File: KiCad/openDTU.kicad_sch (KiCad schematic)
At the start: 48 parts, among them J1 USB_C_Receptacle_USB2.0, J2 Conn_Coaxial, J3 Micro_SD_Card, J4 Conn_02x05_Counter_Clockwise, Q1 BC817, Q2 BC817, SW1 SW_Push, SW2 SW_Push, U1 CH340C, U3 ESP32-WROOM-32, U4 nRF24L01P, U5 NCP1117-3.3_SOT223, Y1 16 MHz

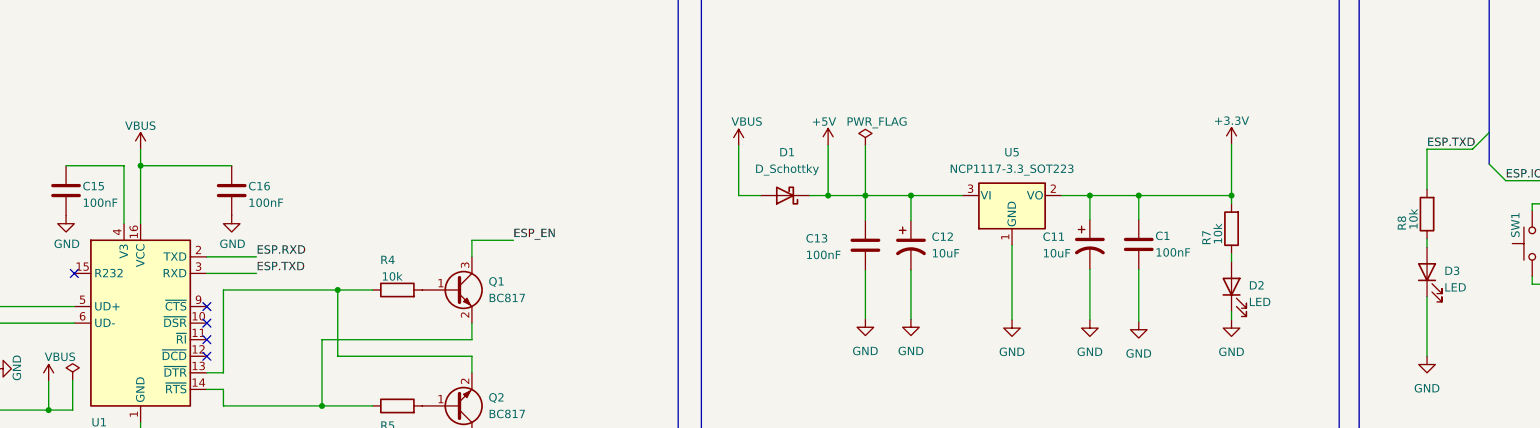
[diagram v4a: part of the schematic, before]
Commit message: fixing bug with wrong voltage at USB-Seriell Interface IC
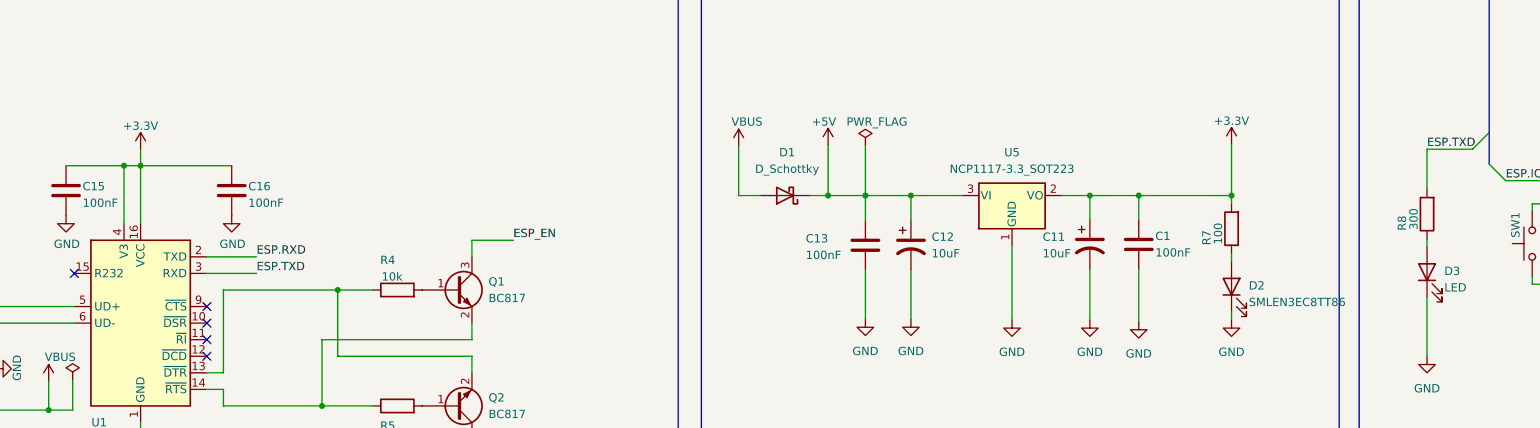
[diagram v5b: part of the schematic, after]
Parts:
- D2: value LED -> SMLEN3EC8TT86
- R7: value 10k -> 100
- R8: value 10k -> 300
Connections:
- net +3.3V: now also C15.1, C16.1, U1.16 (VCC), U1.4 (V3)
- net VBUS: no longer C16.1, U1.16 (VCC)
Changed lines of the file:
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@@
   (junction (at 160.401 51.308) (diameter 0) (color 0 0 0 0)
+  )
+  (junction (at 96.52 188.087) (diameter 0) (color 0 0 0 0)
   )
   (junction (at 305.816 155.956) (diameter 0) (color 0 0 0 0)
@@
     (stroke (width 0) (type default) (color 0 0 0 0))
   )
+  (wire (pts (xy 96.52 188.087) (xy 99.06 188.087))
+    (stroke (width 0) (type default) (color 0 0 0 0))
+  )
   (wire (pts (xy 240.284 192.659) (xy 244.602 192.659))
     (stroke (width 0) (type default) (color 0 0 0 0))
@@
       (effects (font (size 1.27 1.27)) (justify right))
     )
-    (property "Value" "LED" (id 1) (at 268.9606 209.0166 90)
+    (property "Value" "SMLEN3EC8TT86" (id 1) (at 268.9606 209.0166 90)
       (effects (font (size 1.27 1.27)) (justify right))
     )
@@
       (effects (font (size 1.27 1.27)) hide)
     )
-    (property "Datasheet" "~" (id 3) (at 266.319 206.629 0)
+    (property "Datasheet" "https://fscdn.rohm.com/en/products/databook/datasheet/opto/led/chip_mono/smlen3ec8tt86-e.pdf" (id 3) (at 266.319 206.629 0)
       (effects (font (size 1.27 1.27)) hide)
     )
@@
       (effects (font (size 1.27 1.27)) (justify right))
     )
-    (property "Value" "10k" (id 1) (at 264.287 200.152 90)
+    (property "Value" "100" (id 1) (at 264.287 200.152 90)
       (effects (font (size 1.27 1.27)) (justify right))
     )
@@
       (effects (font (size 1.27 1.27)) (justify right))
     )
-    (property "Value" "10k" (id 1) (at 294.259 197.9168 90)
+    (property "Value" "300" (id 1) (at 294.259 197.9168 90)
       (effects (font (size 1.27 1.27)) (justify right))
     )
@@
     (pin "1")
     (pin "2")
-  )
-  (symbol (lib_id "power:VBUS") (at 99.06 185.547 0) (unit 1)
-    (in_bom yes) (on_board yes)
-    (property "Reference" "#PWR018" (id 0) (at 99.06 189.357 0)
-      (effects (font (size 1.27 1.27)) hide)
-    )
-    (property "Value" "VBUS" (id 1) (at 99.06 181.991 0))
-    (property "Footprint" "" (id 2) (at 99.06 185.547 0)
-      (effects (font (size 1.27 1.27)) hide)
-    )
-    (property "Datasheet" "" (id 3) (at 99.06 185.547 0)
-      (effects (font (size 1.27 1.27)) hide)
-    )
-    (pin "1")
   )
   (symbol (lib_id "power:GND") (at 76.708 219.202 90) (unit 1)
@@
     (pin "2")
   )
+  (symbol (lib_id "power:+3.3V") (at 99.06 185.547 0) (unit 1)
+    (in_bom yes) (on_board yes)
+    (property "Reference" "#PWR0116" (id 0) (at 99.06 189.357 0)
+      (effects (font (size 1.27 1.27)) hide)
+    )
+    (property "Value" "+3.3V" (id 1) (at 99.06 181.991 0))
+    (property "Footprint" "" (id 2) (at 99.06 185.547 0)
+      (effects (font (size 1.27 1.27)) hide)
+    )
+    (property "Datasheet" "" (id 3) (at 99.06 185.547 0)
+      (effects (font (size 1.27 1.27)) hide)
+    )
+    (pin "1")
+  )
   (symbol (lib_id "RF:nRF24L01P") (at 160.401 75.438 0) (unit 1)
     (in_bom yes) (on_board yes) (fields_autoplaced)
@@
       (reference "#PWR017") (unit 1) (value "GND") (footprint "")
     )
-    (path "/7131b016-1210-4d20-894c-1b141a415518"
-      (reference "#PWR018") (unit 1) (value "VBUS") (footprint "")
-    )
     (path "/e16ea1ad-3b7c-47e3-883a-76ed6b5aaaaf"
       (reference "#PWR019") (unit 1) (value "GND") (footprint "")
@@
       (reference "#PWR0115") (unit 1) (value "GND") (footprint "")
     )
+    (path "/b6a9a3e1-4557-4747-8eb7-7b753ce33949"
+      (reference "#PWR0116") (unit 1) (value "+3.3V") (footprint "")
+    )
     (path "/883cada5-36b1-4829-bf6c-a23fe5e54384"
       (reference "C1") (unit 1) (value "100nF") (footprint "Capacitor_SMD:C_0603_1608Metric_Pad1.08x0.95mm_HandSolder")
@@
     )
     (path "/2031b417-cd76-4ae8-aaab-2b0c95d0c0af"
-      (reference "D2") (unit 1) (value "LED") (footprint "LED_SMD:LED_0603_1608Metric_Pad1.05x0.95mm_HandSolder")
+      (reference "D2") (unit 1) (value "SMLEN3EC8TT86") (footprint "LED_SMD:LED_0603_1608Metric_Pad1.05x0.95mm_HandSolder")
     )
     (path "/27747454-43e7-428e-a869-660000ce9d89"
@@
     )
     (path "/344cbc84-1e3b-49e4-946c-1eb02cb9f2cd"
-      (reference "R7") (unit 1) (value "10k") (footprint "Resistor_SMD:R_0603_1608Metric")
+      (reference "R7") (unit 1) (value "100") (footprint "Resistor_SMD:R_0603_1608Metric")
     )
     (path "/4954466a-f18e-4b11-80d2-dca4958e8c04"
-      (reference "R8") (unit 1) (value "10k") (footprint "Resistor_SMD:R_0603_1608Metric")
+      (reference "R8") (unit 1) (value "300") (footprint "Resistor_SMD:R_0603_1608Metric")
     )
     (path "/8e233198-1ea8-4a3a-98c0-8d599041add5"
